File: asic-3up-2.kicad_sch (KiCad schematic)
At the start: 64 parts, among them J8 Conn_01x01, J9 Conn_01x01, U57 MCP1824T-1202E/OT, U58 MCP1824T-1202E/OT, U59 MCP1824T-1202E/OT, U60 MCP1824T-0802E, U61 MCP1824T-0802E, U62 MCP1824T-0802E, U63 BM1362AC_MODE1, U64 BM1362AC_MODE0, U65 BM1362AC_MODE1

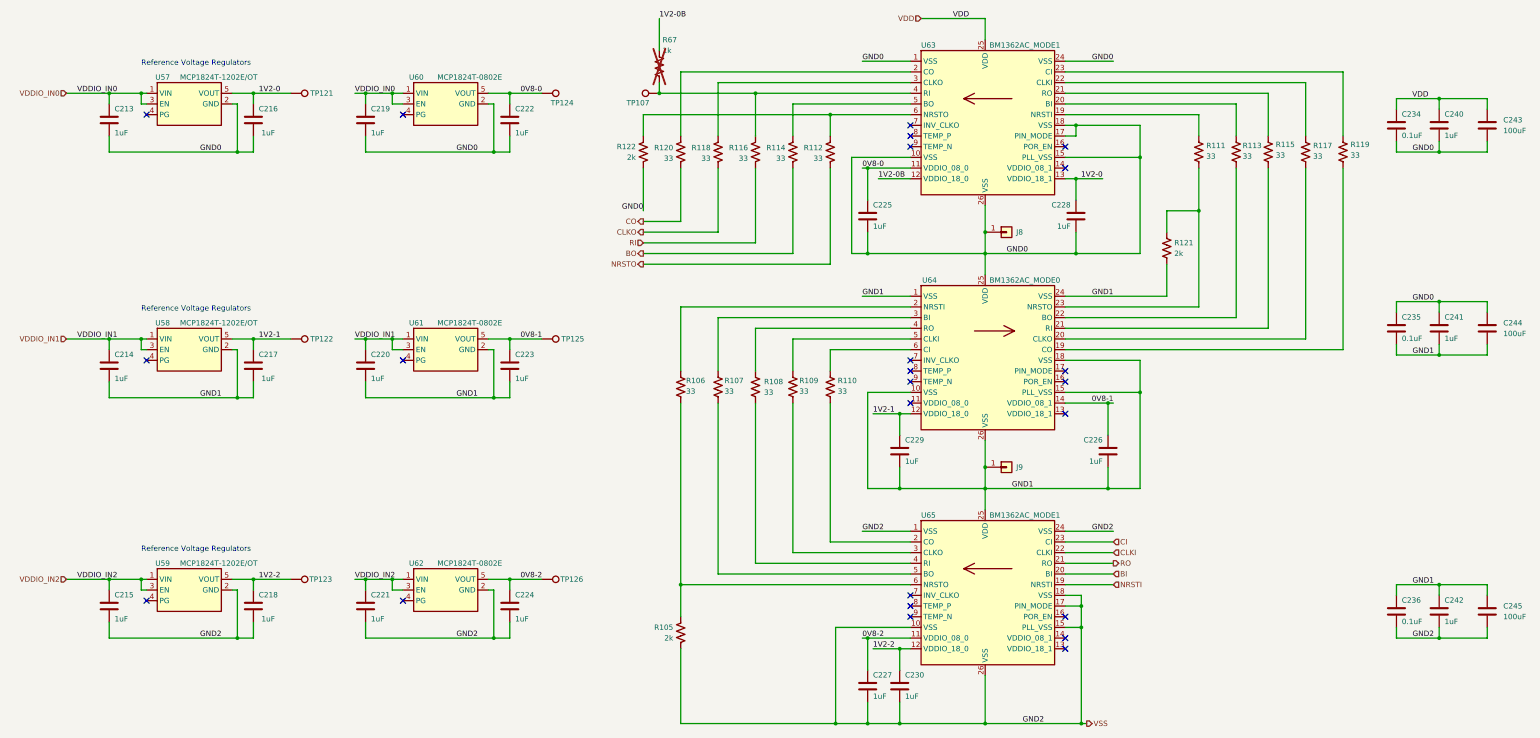
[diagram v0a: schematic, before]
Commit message: added topside data test pads. cleaned up power pads some more.
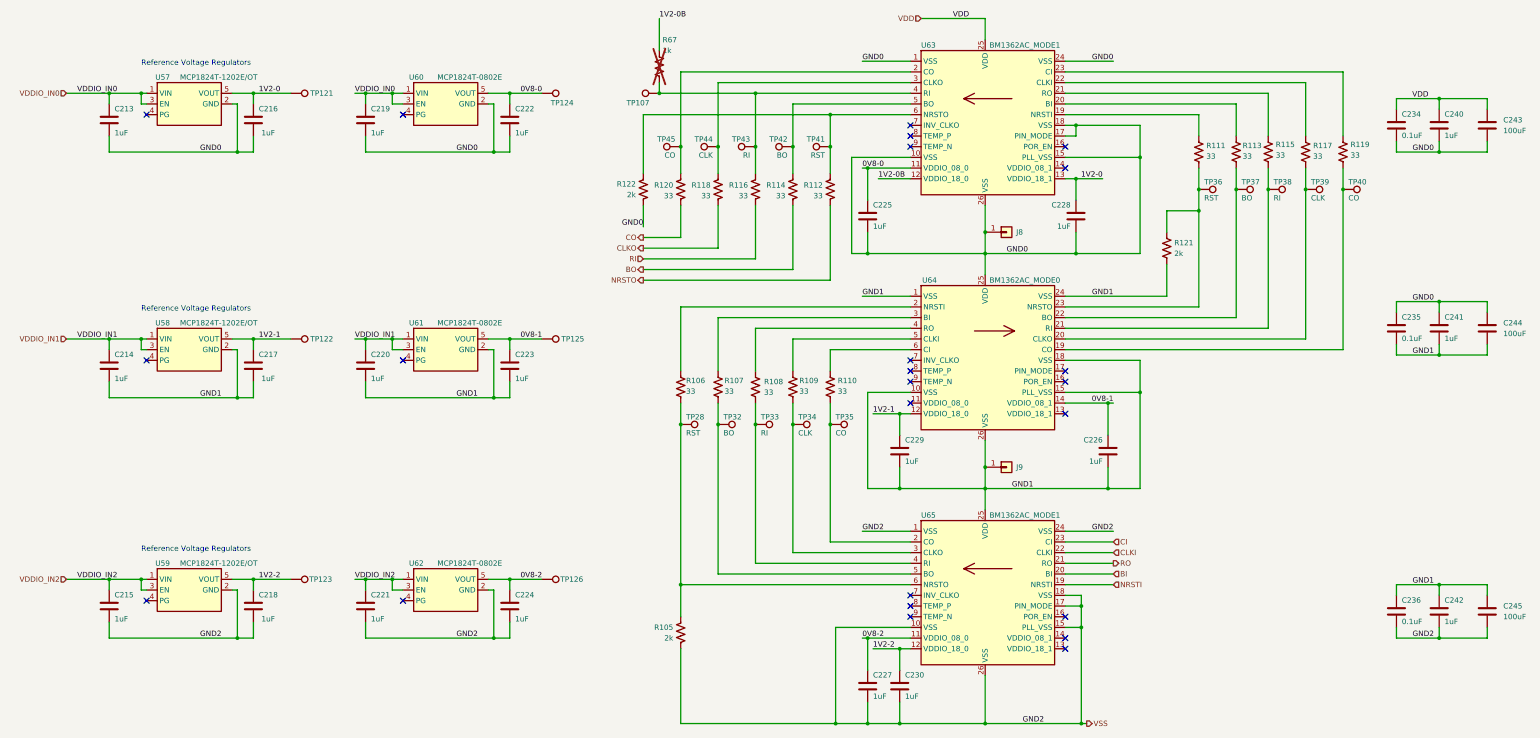
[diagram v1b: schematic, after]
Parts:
- added TP28, TP36, TP41: RST, emberone:TestPoint_Pad_1.0x0.4mm, symbol Connector:TestPoint
- added TP32, TP37, TP42: BO, emberone:TestPoint_Pad_1.0x0.4mm, symbol Connector:TestPoint
- added TP33, TP38, TP43: RI, emberone:TestPoint_Pad_1.0x0.4mm, symbol Connector:TestPoint
- added TP34, TP39, TP44: CLK, emberone:TestPoint_Pad_1.0x0.4mm, symbol Connector:TestPoint
- added TP35, TP40, TP45: CO, emberone:TestPoint_Pad_1.0x0.4mm, symbol Connector:TestPoint
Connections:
- net at R113.2, U64.22 (BO): now also TP37.1
- net at R119.2, U64.19 (CO): now also TP40.1
- net at R110.2, U65.2 (CO): now also TP35.1
- net at R114.1, U63.5 (BO): now also TP42.1
- net at R120.1, U63.2 (CO): now also TP45.1
- net at R118.1, U63.3 (CLKO): now also TP44.1
- net at R116.1, R67.2, TP107.1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: now also TP43.1
- net at R112.1, R122.1, U63.6 (NRSTO): now also TP41.1
- net at R111.2, R121.1, U64.23 (NRSTO): now also TP36.1
- net at R117.2, U64.20 (CLKO): now also TP39.1
- net at R115.2, U64.21 (RI): now also TP38.1
- net at R109.2, U65.3 (CLKO): now also TP34.1
- net at R108.2, U65.4 (RI): now also TP33.1
- net at R107.2, U65.5 (BO): now also TP32.1
- net at R105.1, R106.2, U65.6 (NRSTO): now also TP28.1
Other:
- moved on the sheet: R112, R114, R116, R118, R120, R122

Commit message: add BOM, iBOM and position files
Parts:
- J8, J9: now left out of the parts list
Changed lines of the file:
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@@
 		(unit 1)
 		(exclude_from_sim no)
-		(in_bom yes)
+		(in_bom no)
 		(on_board yes)
 		(dnp no)
@@
 		(unit 1)
 		(exclude_from_sim no)
-		(in_bom yes)
-		(on_board yes)
-		(dnp no)
+		(in_bom no)
+		(on_board yes)
+		(dnp no)

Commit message: corrected the voltage regulator input and output capacitors. Updated BOM, iBOM, cpos, gerbers and render.
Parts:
- U63, U64, U65: PARTNO (none) -> BM1362AC
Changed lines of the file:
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@@
 			)
 		)
+		(property "PARTNO" "BM1362AC"
+			(at 248.92 182.88 0)
+			(effects
+				(font
+					(size 1.27 1.27)
+				)
+				(hide yes)
+			)
+		)
 		(pin "12"
 		)
@@
 			)
 		)
+		(property "PARTNO" "BM1362AC"
+			(at 248.92 71.12 0)
+			(effects
+				(font
+					(size 1.27 1.27)
+				)
+				(hide yes)
+			)
+		)
 		(pin "12"
 		)
@@
 			(at 248.92 127 0)
 			(effects
+				(font
+					(size 1.27 1.27)
+				)
+				(hide yes)
+			)
+		)
+		(property "PARTNO" "BM1362AC"
+			(at 248.92 127 0)
+			(effects

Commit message: bump version to v6
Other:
- company: (none) -> 256Foundation
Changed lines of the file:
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@@
 	(title_block
 		(title "emberOne/00")
-		(date "2025-09-17")
-		(rev "5")
+		(date "2026-02-17")
+		(rev "v6")
+		(company "256Foundation")
+		(comment 1 "OHL-S-2.0")
 	)
 	(text "Reference Voltage Regulators"
